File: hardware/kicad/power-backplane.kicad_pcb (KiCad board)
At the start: 2 copper layers, 150 x 95 mm, 18 parts, among them P501 I/O board power, P502 Tank board power, P503 Crossfade board power, P504 Filter board power, P505 Spare utility power, P506 Ext-routing board power, P601 Control-backplane power

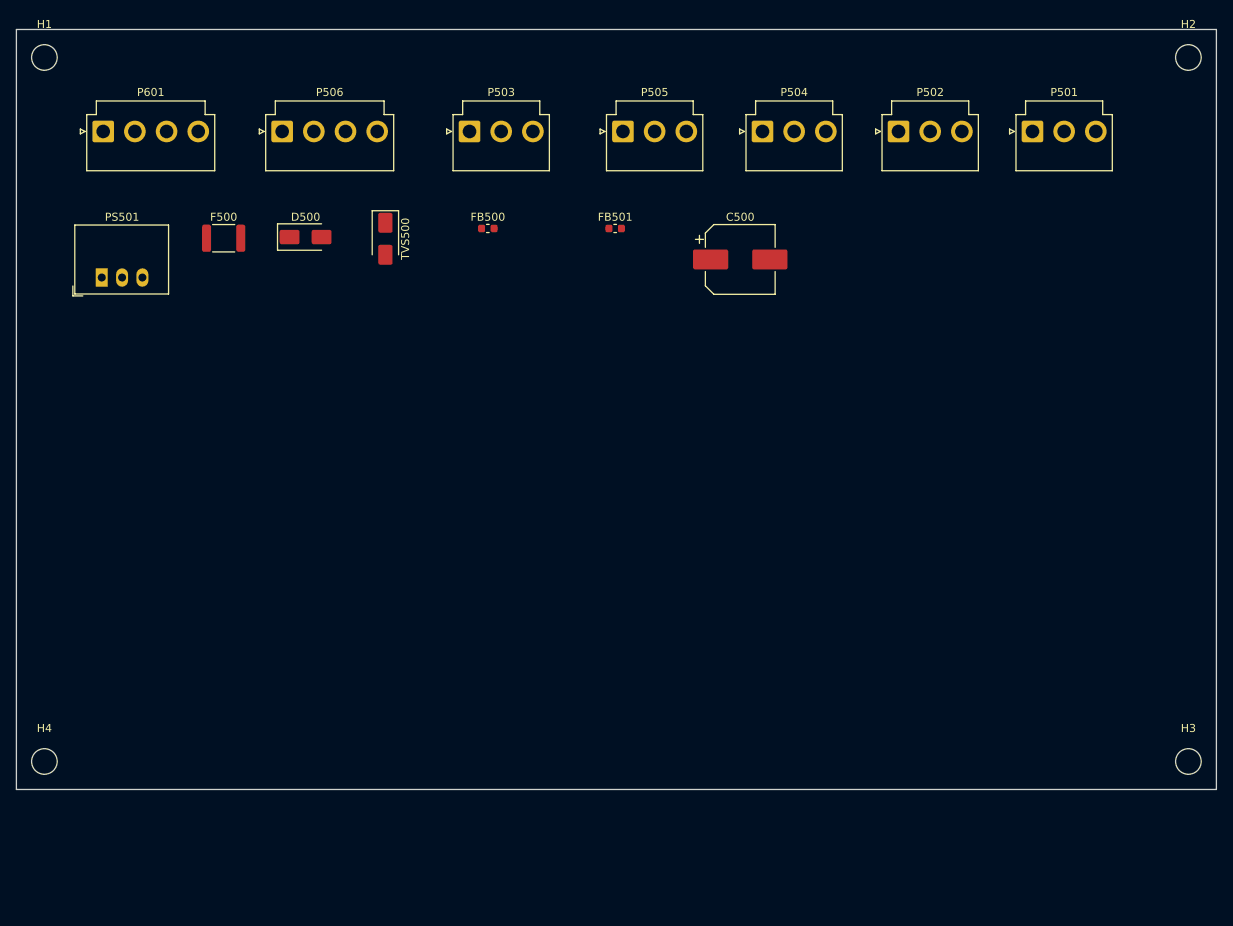
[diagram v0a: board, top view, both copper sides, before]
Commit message: Board 2 power-backplane: ERC 0, ripple-filter sim -50dB @350kHz verified, routed PCB DRC 0/0, fab outputs; URB->URA2415YMD-10WR3 part correction (URB is single-output)
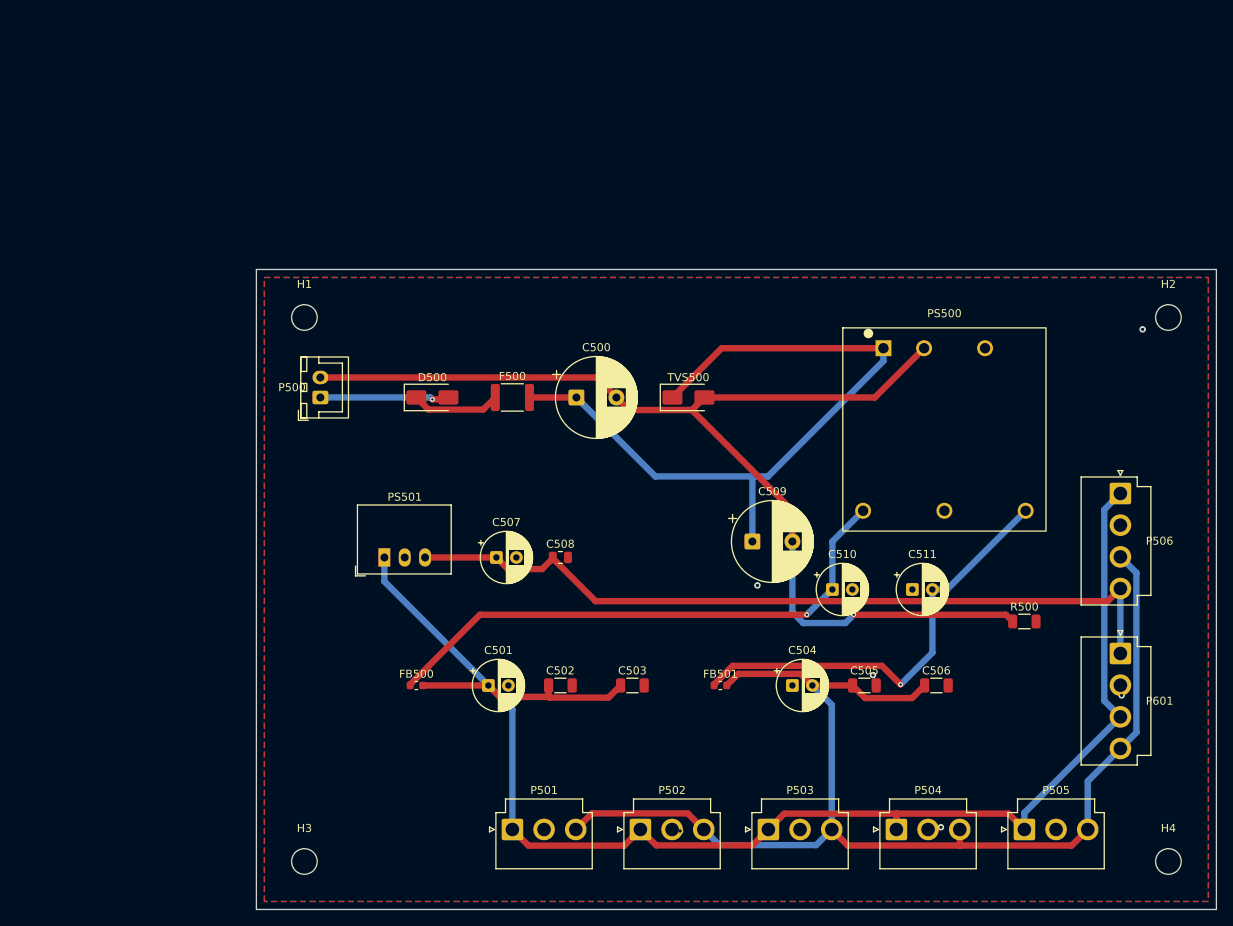
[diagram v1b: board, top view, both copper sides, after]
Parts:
- added C501: 100u, Capacitor_THT:CP_Radial_D6.3mm_P2.50mm, F.Cu at (59.0, 82.0)
- added C502: 10u, Capacitor_SMD:C_1206_3216Metric, F.Cu at (68.0, 82.0)
- added C503: 100n, Capacitor_SMD:C_1206_3216Metric, F.Cu at (77.0, 82.0)
- added C504: 100u, Capacitor_THT:CP_Radial_D6.3mm_P2.50mm, F.Cu at (97.0, 82.0)
- added C505: 10u, Capacitor_SMD:C_1206_3216Metric, F.Cu at (106.0, 82.0)
- added C506: 100n, Capacitor_SMD:C_1206_3216Metric, F.Cu at (115.0, 82.0)
- added C507: 47u, Capacitor_THT:CP_Radial_D6.3mm_P2.50mm, F.Cu at (60.0, 66.0)
- added C508: 100n, Capacitor_SMD:C_0805_2012Metric, F.Cu at (68.0, 66.0)
- added C509: 100u, Capacitor_THT:CP_Radial_D10.0mm_P5.00mm, F.Cu at (92.0, 64.0)
- added C510: 10u, Capacitor_THT:CP_Radial_D6.3mm_P2.50mm, F.Cu at (102.0, 70.0)
- added C511: 10u, Capacitor_THT:CP_Radial_D6.3mm_P2.50mm, F.Cu at (112.0, 70.0)
- added P500: P500, Connector_JST:JST_XH_B2B-XH-A_1x02_P2.50mm_Vertical, F.Cu at (38.0, 46.0)
- added PS500: URA2415YMD-10WR3, GAS:URA_YMD-10WR3, F.Cu at (116.0, 50.0)
- added R500: 0, Resistor_SMD:R_1206_3216Metric, F.Cu at (126.0, 74.0)
- C500: value 220u/25V -> 220u; footprint CP_Elec_8x10.5 -> Capacitor_THT:CP_Radial_D10.0mm_P5.00mm
- D500, TVS500: footprint D_SMA -> Diode_SMD:D_SMA
- F500: value MF-R100 -> 1.1A PTC MF-MSMF110; footprint Fuse_1812_4532Metric -> Fuse:Fuse_1812_4532Metric
- FB500, FB501: footprint L_0603_1608Metric -> Inductor_SMD:L_0603_1608Metric
- H1, H2, H3, H4: value M3 NPTH -> M3; footprint MountingHole_3.2mm_M3 -> MountingHole:MountingHole_3.2mm_M3
- P501: value I/O board power -> P501; footprint JST_VH_B3P-VH_1x03_P3.96mm_Vertical -> Connector_JST:JST_VH_B3P-VH_1x03_P3.96mm_Vertical
- P502: value Tank board power -> P502; footprint JST_VH_B3P-VH_1x03_P3.96mm_Vertical -> Connector_JST:JST_VH_B3P-VH_1x03_P3.96mm_Vertical
- P503: value Crossfade board power -> P503; footprint JST_VH_B3P-VH_1x03_P3.96mm_Vertical -> Connector_JST:JST_VH_B3P-VH_1x03_P3.96mm_Vertical
- P504: value Filter board power -> P504; footprint JST_VH_B3P-VH_1x03_P3.96mm_Vertical -> Connector_JST:JST_VH_B3P-VH_1x03_P3.96mm_Vertical
- P505: value Spare utility power -> P505; footprint JST_VH_B3P-VH_1x03_P3.96mm_Vertical -> Connector_JST:JST_VH_B3P-VH_1x03_P3.96mm_Vertical
- P506: value Ext-routing board power -> P506; footprint JST_VH_B4P-VH_1x04_P3.96mm_Vertical -> Connector_JST:JST_VH_B4P-VH_1x04_P3.96mm_Vertical
- P601: value Control-backplane power -> P601; footprint JST_VH_B4P-VH_1x04_P3.96mm_Vertical -> Connector_JST:JST_VH_B4P-VH_1x04_P3.96mm_Vertical
- PS501: footprint Converter_DCDC_RECOM_R-78E-0.5_THT -> Converter_DCDC:Converter_DCDC_RECOM_R-78E-0.5_THT
- moved P601 142.9 mm to (138.0, 78.0), turned to -90 degrees
- moved H4 141.1 mm to (144.0, 104.0)
- moved P506 114.1 mm to (138.0, 58.0), turned to -90 degrees
- moved H3 111.2 mm to (36.0, 104.0)
- moved P501 108.8 mm to (62.0, 100.0)
- moved P505 100.7 mm to (126.0, 100.0)
- moved P503 94.9 mm to (94.0, 100.0)
- moved P502 93.0 mm to (78.0, 100.0)
- moved P504 88.8 mm to (110.0, 100.0)
- moved FB501 58.6 mm to (88.0, 82.0)
- moved FB500 57.8 mm to (50.0, 82.0)
- moved PS501 49.7 mm to (46.0, 66.0)
- moved H1 46.0 mm to (36.0, 36.0)
- moved TVS500 42.8 mm to (84.0, 46.0), turned to 0 degrees
- moved F500 41.2 mm to (62.0, 46.0)
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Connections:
- C500 pad 1: (no net) -> +30V_F
- C500 pad 2: (no net) -> GND_IN
- D500 pad 1: (no net) -> +30V_D
- D500 pad 2: (no net) -> +30V_RAW
- F500 pad 1: (no net) -> +30V_D
- F500 pad 2: (no net) -> +30V_F
- FB500 pad 1: (no net) -> +15VRAW
- FB500 pad 2: (no net) -> +15VA
- FB501 pad 1: (no net) -> -15VRAW
- FB501 pad 2: (no net) -> -15VA
- P501 pad 1: (no net) -> +15VA
- P501 pad 2: (no net) -> AGND
- P501 pad 3: (no net) -> -15VA
- P502 pad 1: (no net) -> +15VA
- P502 pad 2: (no net) -> AGND
- P502 pad 3: (no net) -> -15VA
- P503 pad 1: (no net) -> +15VA
- P503 pad 2: (no net) -> AGND
- P503 pad 3: (no net) -> -15VA
- P504 pad 1: (no net) -> +15VA
- P504 pad 2: (no net) -> AGND
- P504 pad 3: (no net) -> -15VA
- P505 pad 1: (no net) -> +15VA
- P505 pad 2: (no net) -> AGND
- P505 pad 3: (no net) -> -15VA
- P506 pad 1: (no net) -> +15VA
- P506 pad 2: (no net) -> AGND
- P506 pad 3: (no net) -> -15VA
- P506 pad 4: (no net) -> +5VAUX
- P601 pad 1: (no net) -> +5VAUX
- P601 pad 2: (no net) -> AGND
- P601 pad 3: (no net) -> +15VA
- P601 pad 4: (no net) -> -15VA
- PS501 pad 1: (no net) -> +15VA
- PS501 pad 2: (no net) -> AGND
- PS501 pad 3: (no net) -> +5VAUX
- TVS500 pad 1: (no net) -> +30V_F
- TVS500 pad 2: (no net) -> GND_IN
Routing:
- net +15VA: track 0.00 -> 187.6 mm
- net -15VA: track 0.00 -> 154.6 mm
- net GND_IN: track 0.00 -> 139.7 mm, vias 0 -> 1
- net +5VAUX: track 0.00 -> 99.2 mm
- net +30V_F: track 0.00 -> 93.0 mm
- net +15VRAW: track 0.00 -> 69.3 mm, vias 0 -> 1
- net -15VRAW: track 0.00 -> 54.6 mm, vias 0 -> 1
- net +30V_RAW: track 0.00 -> 16.2 mm, vias 0 -> 1
- net +30V_D: track 0.00 -> 11.1 mm
- net AGND: vias 0 -> 6
- added copper zone on B.Cu, net AGND
- added copper zone on F.Cu, net AGND
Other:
- board size 150 x 95 mm -> 120 x 80 mm
- board text removed: "GAS Rev A - Power / Backplane Board"
- board text removed: "OUTLINE SCAFFOLD - NOT FOR FAB"

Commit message: Schematic review (kicad-schematic-review skill): F1 R-78E moved to +15VRAW, F2 mono-float bleed R25; both boards re-routed/verified; datasheet cache, per-instance reviews, schematic_review.md
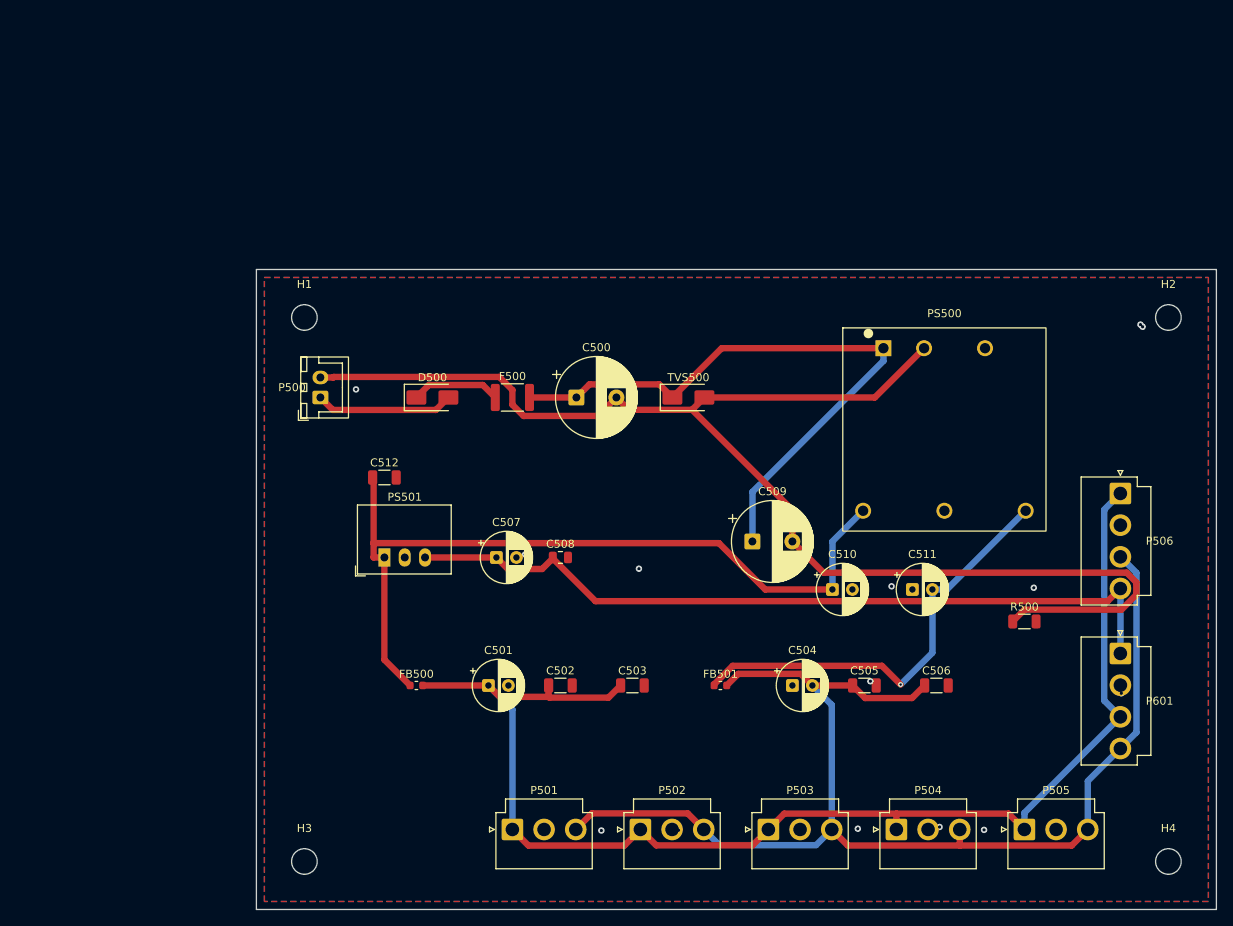
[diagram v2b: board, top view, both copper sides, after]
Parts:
- removed the R500 at (126.0, 74.0)
- added H1: M3, MountingHole:MountingHole_3.2mm_M3, F.Cu at (36.0, 36.0)
- added P501: P501, Connector_JST:JST_VH_B3P-VH_1x03_P3.96mm_Vertical, F.Cu at (62.0, 100.0)
- C512: renamed from D500; value SS34 -> 10u; footprint Diode_SMD:D_SMA -> Capacitor_SMD:C_1206_3216Metric
- D500: renamed from F500; value 1.1A PTC MF-MSMF110 -> SS34; footprint Fuse:Fuse_1812_4532Metric -> Diode_SMD:D_SMA
- F500: renamed from FB500; value BLM18PG471SN1 -> 1.1A PTC MF-MSMF110; footprint Inductor_SMD:L_0603_1608Metric -> Fuse:Fuse_1812_4532Metric
- FB501: renamed from P500; value P500 -> BLM18PG471SN1; footprint Connector_JST:JST_XH_B2B-XH-A_1x02_P2.50mm_Vertical -> Inductor_SMD:L_0603_1608Metric
- P500: renamed from P501; value P501 -> P500; footprint Connector_JST:JST_VH_B3P-VH_1x03_P3.96mm_Vertical -> Connector_JST:JST_XH_B2B-XH-A_1x02_P2.50mm_Vertical
- R500: renamed from TVS500; value SMAJ33A -> 0; footprint Diode_SMD:D_SMA -> Resistor_SMD:R_1206_3216Metric
- TVS500: renamed from H1; value M3 -> SMAJ33A; footprint MountingHole:MountingHole_3.2mm_M3 -> Diode_SMD:D_SMA
- moved FB501 61.6 mm to (88.0, 82.0), turned to 0 degrees
- moved P500 59.1 mm to (38.0, 46.0), turned to 90 degrees
- moved R500 50.5 mm to (126.0, 74.0)
- moved TVS500 49.0 mm to (84.0, 46.0)
- moved FB500 38.0 mm to (50.0, 82.0)
- moved F500 37.9 mm to (62.0, 46.0)
- moved C512 11.7 mm to (46.0, 56.0)
- moved D500 10.0 mm to (52.0, 46.0)
- renumbered FB501 to FB500
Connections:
- C512 pad 1: +30V_D -> +15VRAW
- C512 pad 2: +30V_RAW -> AGND
- D500 pad 2: +30V_F -> +30V_RAW
- F500 pad 1: +15VRAW -> +30V_D
- F500 pad 2: +15VA -> +30V_F
- FB500 pad 1: -15VRAW -> +15VRAW
- FB500 pad 2: -15VA -> +15VA
- FB501 pad 1: +30V_RAW -> -15VRAW
- FB501 pad 2: GND_IN -> -15VA
- P500 pad 1: +15VA -> +30V_RAW
- P500 pad 2: AGND -> GND_IN
- PS501 pad 1: +15VA -> +15VRAW
- R500 pad 1: +30V_F -> GND_IN
- R500 pad 2: GND_IN -> AGND
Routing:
- net +15VRAW: track 69.3 -> 99.9 mm, vias 1 -> 0
- net GND_IN: track 139.7 -> 168.5 mm, vias 1 -> 0
- net +15VA: track 187.6 -> 166.2 mm
- net +30V_F: track 93.0 -> 79.1 mm
- net +30V_RAW: track 16.2 -> 17.3 mm, vias 1 -> 0
- net AGND: vias 6 -> 14
